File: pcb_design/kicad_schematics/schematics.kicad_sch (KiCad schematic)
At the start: 19 parts, among them J1 Conn_01x05_Pin, J2 LED-HSF08A/B, J3 SG90_01x03_Pin, J4 PICKIT_01x05_Pin, J5 BUTTON-HS-KEY1B, U1 PIC24FJ64GA702-I_SO, U2 ESP8266-01_ESP-01, U3 LM1117LD-3.3

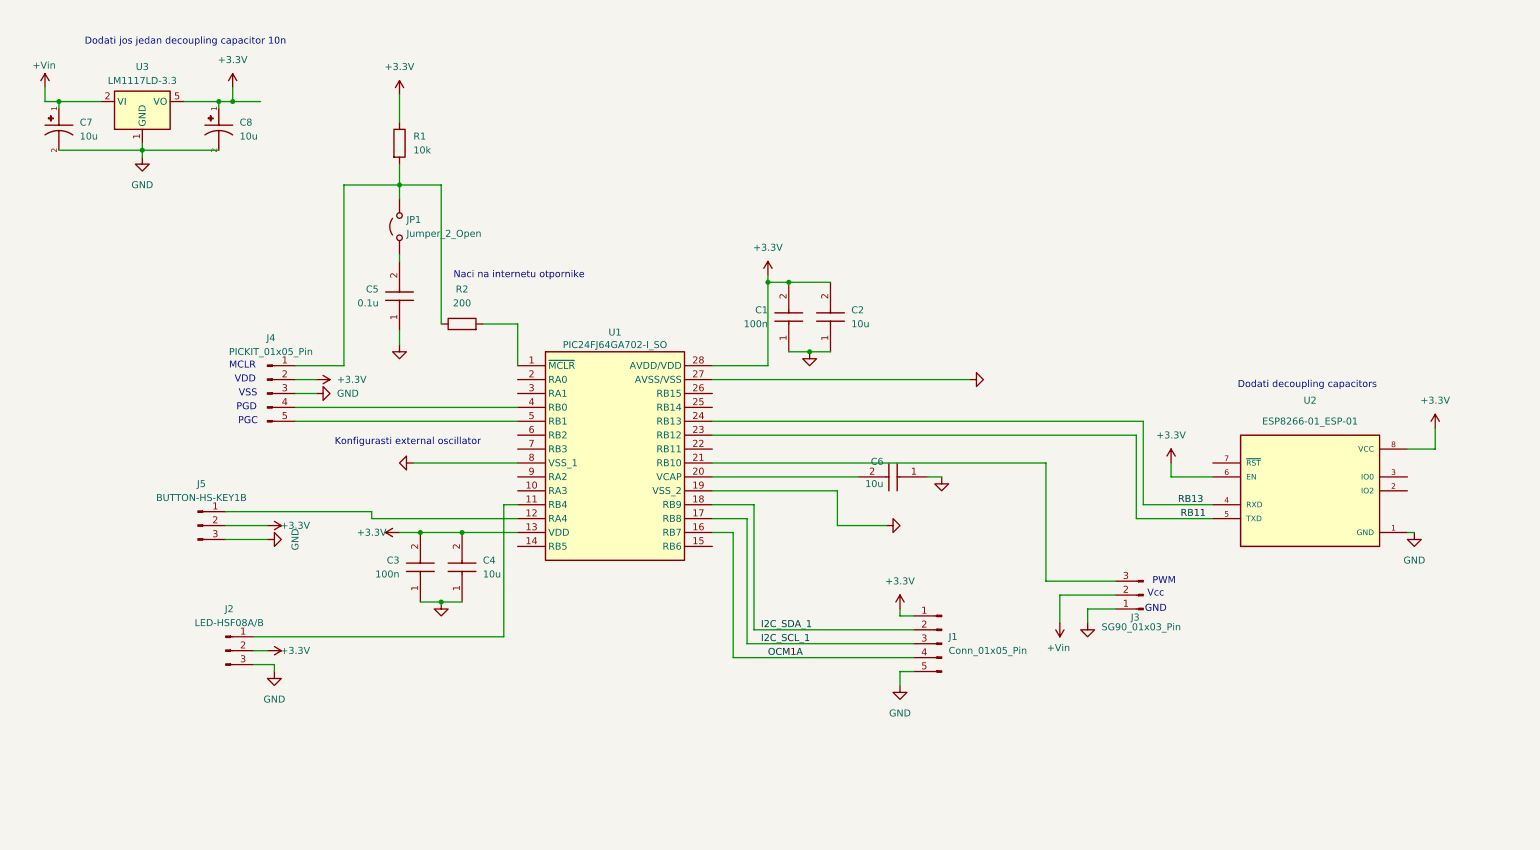
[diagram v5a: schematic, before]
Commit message: Dodani decoupling kondenzatori kod wifi modula i regulatora
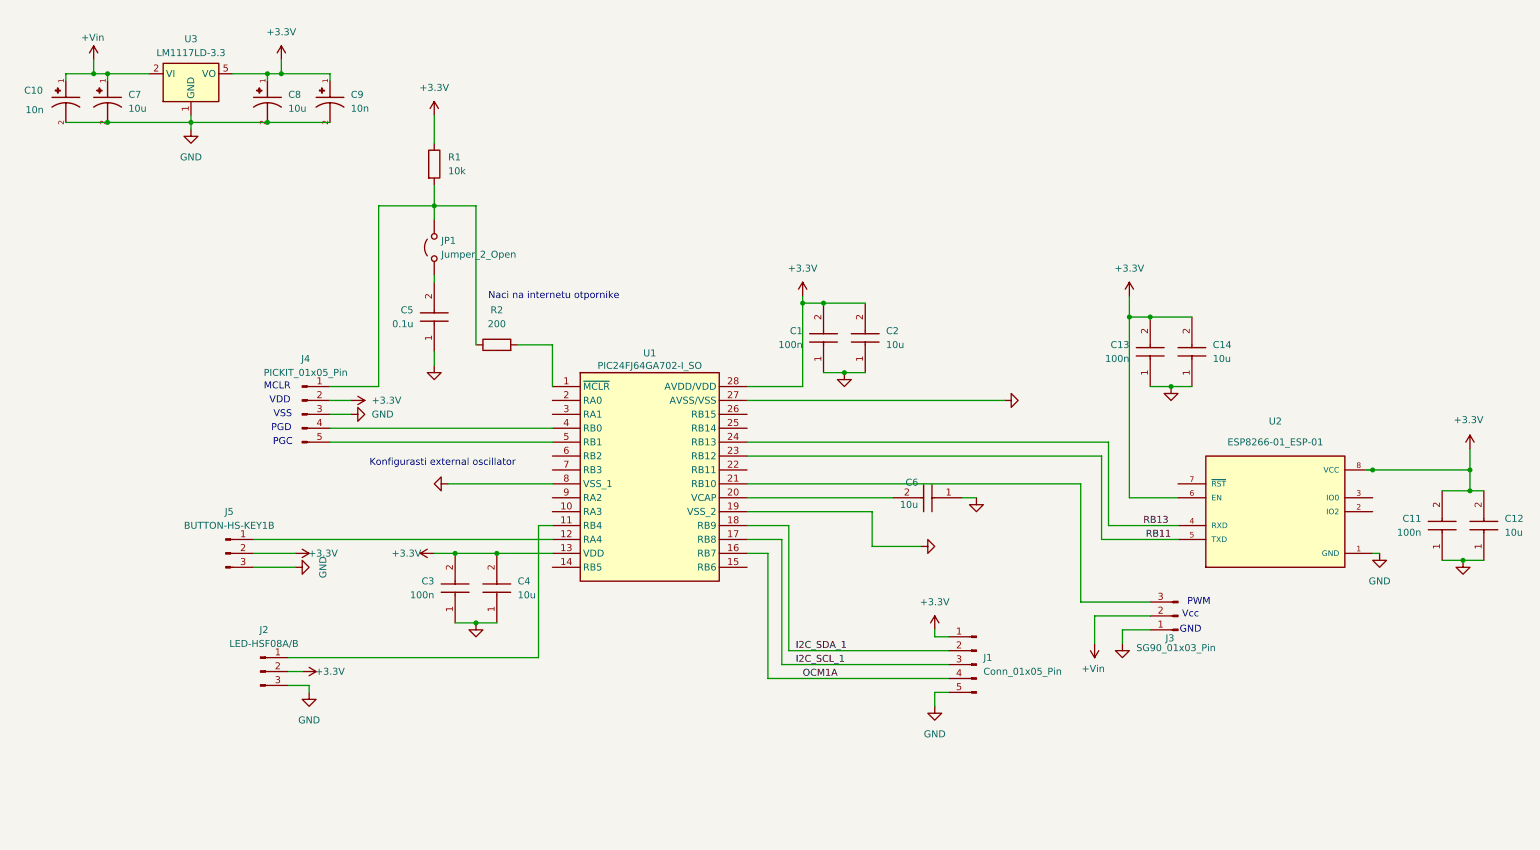
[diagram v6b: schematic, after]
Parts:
- added C10, C9: 10n, T495B106K025ATE750:CAPPC3528X210N, symbol T495B106K025ATE750:T495B106K025ATE750
- added C11, C13: 100n, CAPC2012X145N, symbol CL21X107MRYN3WE:CL21X107MRYN3WE
- added C12, C14: 10u, C0805, symbol C0805C106M4PACTU:C0805C106M4PACTU
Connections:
- net +3.3V: now also C11.2, C12.2, C13.2, C14.2, C9.1
- net +Vin: now also C10.1
- net GND: now also C10.2, C11.1, C12.1, C13.1, C14.1, C9.2
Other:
- note removed: "Dodati decoupling capacitors"
- note removed: "Dodati jos jedan decoupling capacitor 10n"
- moved on the sheet: C1, C2, C3, C4, C5, C6, C7, C8, J1, J2, J3, J4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

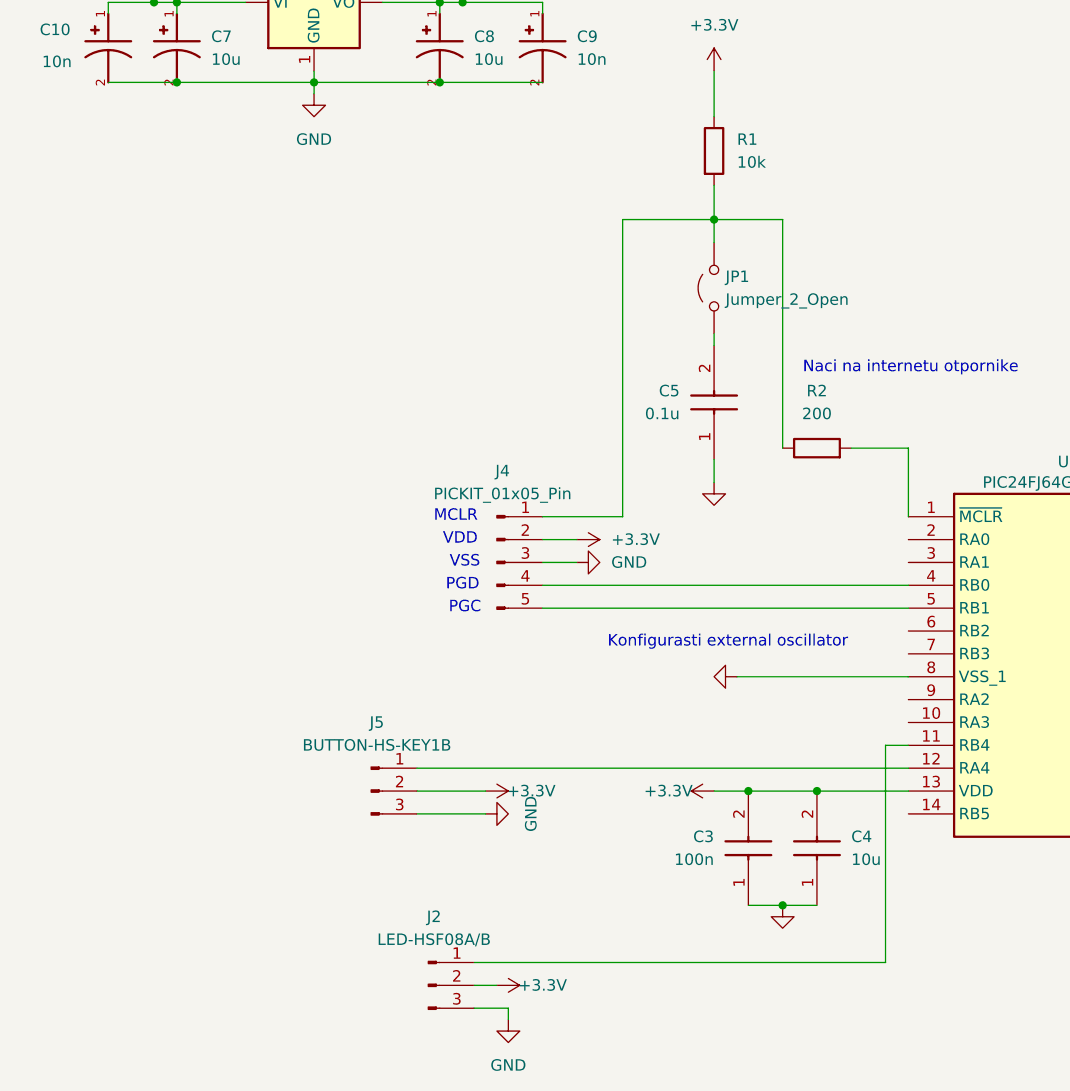
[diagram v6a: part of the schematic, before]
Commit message: Dodan eksterni oscilator
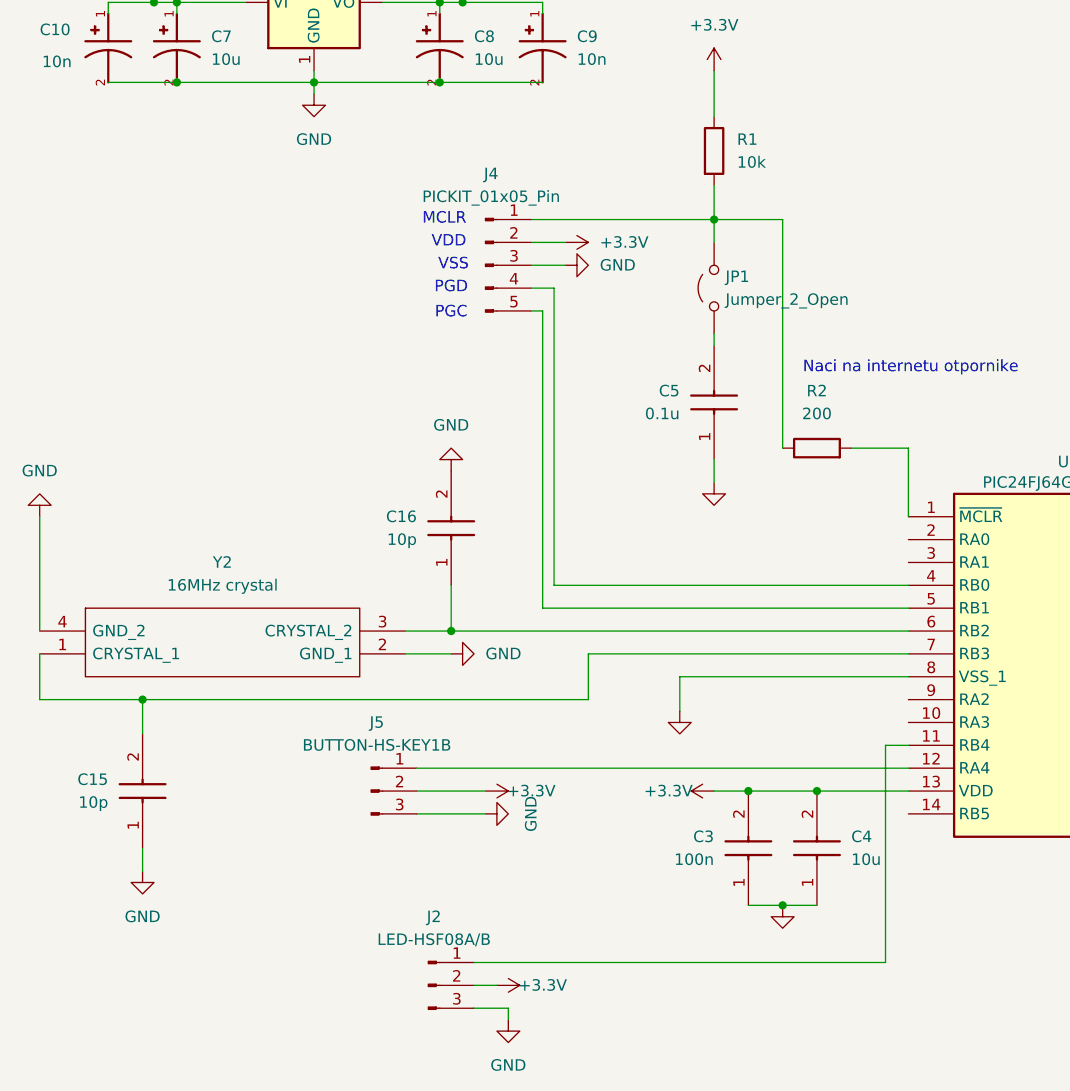
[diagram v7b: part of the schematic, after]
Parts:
- added C15, C16: 10p, CAPC2012X145N, symbol CL21X107MRYN3WE:CL21X107MRYN3WE
- added Y2: 16MHz crystal, 830108288709, symbol 830108288709:830108288709
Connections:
- net GND: now also C15.1, C16.2, Y2.2 (GND_1), Y2.4 (GND_2)
- net at U1.6 (RB2): now also C16.1, Y2.3 (CRYSTAL_2)
- net at U1.7 (RB3): now also C15.2, Y2.1 (CRYSTAL_1)
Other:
- note removed: "Konfigurasti external oscillator"
- moved on the sheet: J4

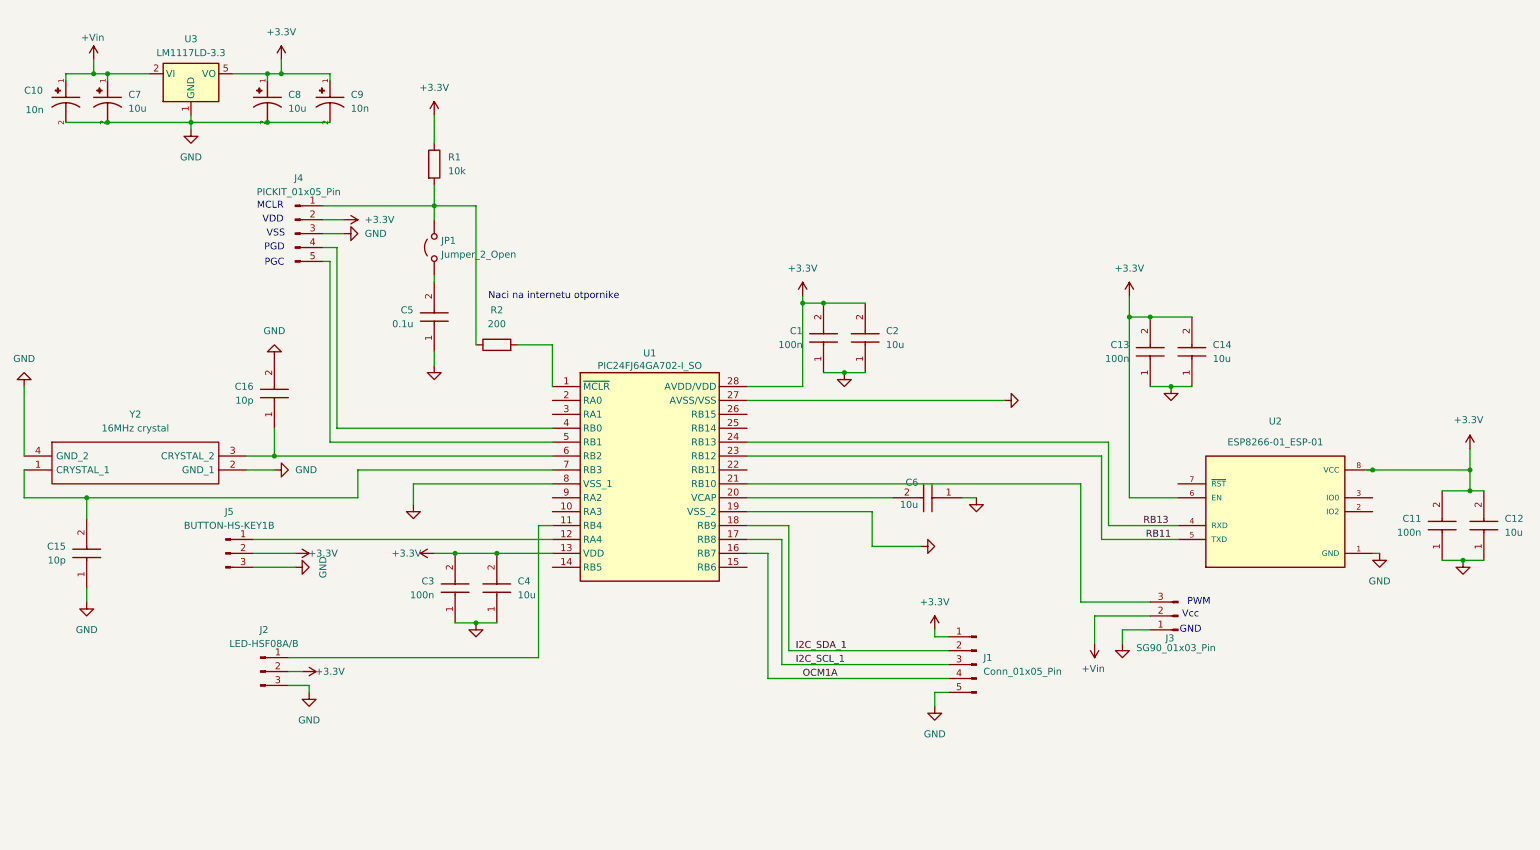
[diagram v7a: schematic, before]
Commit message: Dodani pin headers i odgovarajući modeli koji se koriste u šemi
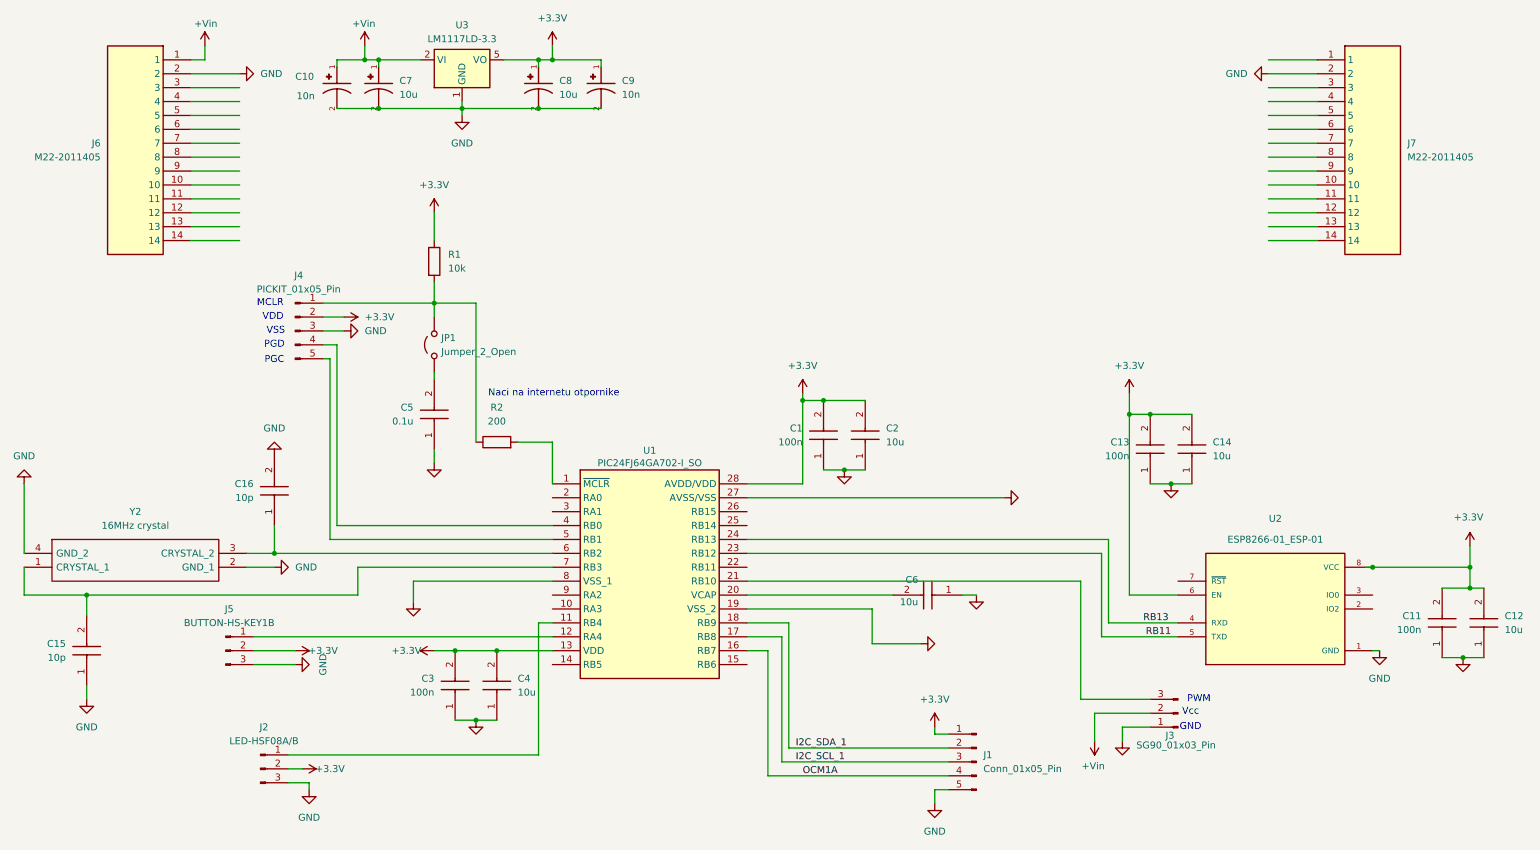
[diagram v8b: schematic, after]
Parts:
- added J6, J7: M22-2011405, HDRV14W50P0X200_1X14_2800X200X525P, symbol 14_pin_Male:M22-2011405
- C1, C11, C13, C3: footprint CAPC2012X145N -> C_Ceramic-100nF:C0402
- C12, C2, C4, C6: footprint C0805 -> C_Ceramic-10uF:C0805
- C5: footprint C0805 -> C_Ceramic-100nF:C0402
- C7, C8: footprint T495B106K025ATE750:CAPPC3528X210N -> C_Polarized_Tantalum-10uF:CAPPC3528X210N
- U1: footprint SOIC127P1030X265-28N -> Microcontroller-PIC24FJ64GA702-I_SO:SOIC127P1030X265-28N
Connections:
- net +Vin: now also J6.1
- net GND: now also J6.2, J7.2
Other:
- moved on the sheet: C1, C10, C11, C12, C13, C14, C15, C16, C2, C3, C4, C5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
